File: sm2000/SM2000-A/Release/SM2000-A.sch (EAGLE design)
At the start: 455 parts, among them CN1 HDR100-3, CN2 ST-3509, CN3 HDR100-3, CN4 JS-MU3-002, CN5 DS-0518, CN6 ST-3509, CN7 ST-3509, J1 JMP-2PIN, J10 JMPR-2X2, J11 JMPR-2X2, J12 JMPR-2X2, J13 JMPR-2X2, J14 JMPR-2X2, J2 HDR100-7, J3 JMP-2PIN, J4 CONN-BOOM-XH-2A, J5 JMP-2PIN, J6 JMPR-2X2, J7 JMPR-2X2, J8 JMPR-2X2, J9 JMPR-2X2, P6 TPAD50, P7 TPAD50, P8 TPAD50, P9 TPAD50, Q1 MMBT3904, Q10 MMBT3904, Q11 BFR92, Q12 BFQ19, Q13 RD01MUS2, Q14 MMBT3904, Q15 MMBT3904, Q16 MMBT3904, Q17 MMBT3906, Q2 STR2P3LLH6, Q3 MMBT3904, Q4 STR2P3LLH6, Q5 MMBT3904, Q6 MMBT3904, Q7 MMBT3904, Q8 MMBT3904, Q9 MMBT3904, SW1 TS-02B, SW2 SW-LC2259, SW3 TS-026, SW4 TS-026, SW5 SW-LC2259EENP, U1 STM32F405VGT6, U10 LM386M-1, U11 ADE-1, U12 PGA-103+, U13 LMV341, U14 SI5351A, U15 SI570, U16 SA612A, U2 STMPS2141, U3 EMIF02-USB03F2, U4 DNL, U5 L78M09, U6 LD1117AS-33, U7 LMV341, U8 LD1117AS-33, U9 TPS54329E, X1 BU-SMA-H

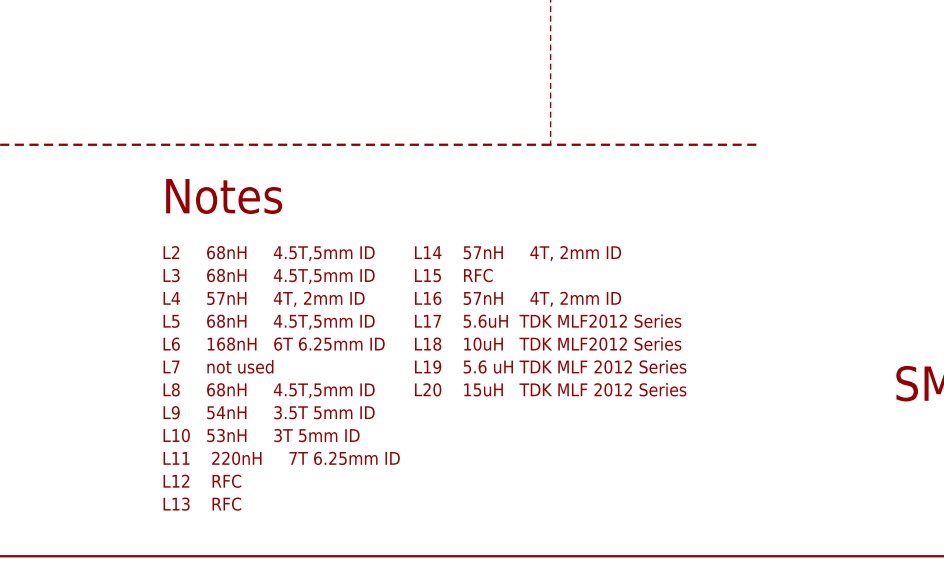
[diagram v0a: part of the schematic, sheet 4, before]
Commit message: SM2000-A Folders should now be current. RGB
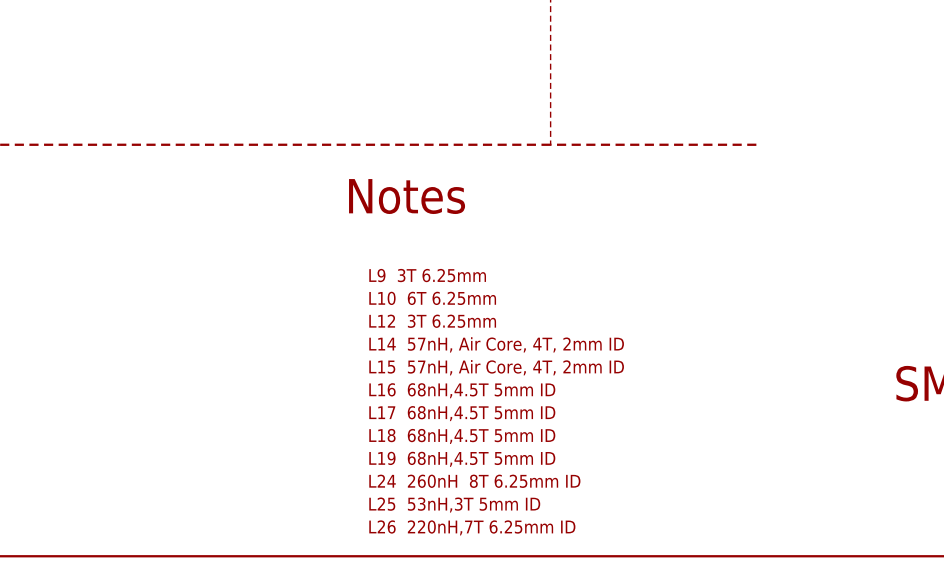
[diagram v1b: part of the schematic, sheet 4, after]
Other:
- note added: "L10 6T 6.25mm"
- note added: "L12 3T 6.25mm"
- note added: "L14 57nH, Air Core, 4T, 2mm ID"
- note added: "L15 57nH, Air Core, 4T, 2mm ID"
- note added: "L16 68nH,4.5T 5mm ID"
- note added: "L17 68nH,4.5T 5mm ID"
- note added: "L18 68nH,4.5T 5mm ID"
- note added: "L19 68nH,4.5T 5mm ID"
- note added: "L24 260nH 8T 6.25mm ID"
- note added: "L25 53nH,3T 5mm ID"
- note added: "L26 220nH,7T 6.25mm ID"
- note added: "L9 3T 6.25mm"
- note removed: "L10 53nH 3T 5mm ID"
- note removed: "L11 220nH 7T 6.25mm ID"
- note removed: "L12 RFC"
- note removed: "L13 RFC"
- note removed: "L14 57nH 4T, 2mm ID"
- note removed: "L15 RFC"
- note removed: "L16 57nH 4T, 2mm ID"
- note removed: "L17 5.6uH TDK MLF2012 Series"
- note removed: "L18 10uH TDK MLF2012 Series"
- note removed: "L19 5.6 uH TDK MLF 2012 Series"
- note removed: "L2 68nH 4.5T,5mm ID"
- note removed: "L20 15uH TDK MLF 2012 Series"
- note removed: "L3 68nH 4.5T,5mm ID"
- note removed: "L4 57nH 4T, 2mm ID"
- note removed: "L5 68nH 4.5T,5mm ID"
- note removed: "L6 168nH 6T 6.25mm ID"
- note removed: "L7 not used"
- note removed: "L8 68nH 4.5T,5mm ID"
- note removed: "L9 54nH 3.5T 5mm ID"
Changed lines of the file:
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@@
 <text x="345.44" y="17.272" size="3.81" layer="94" ratio="10">SM2000 - </text>
 <text x="422.148" y="6.35" size="3.81" layer="94" ratio="10">A</text>
+<text x="287.02" y="27.94" size="1.4224" layer="94">L10  6T 6.25mm</text>
+<text x="287.02" y="25.4" size="1.4224" layer="94">L12  3T 6.25mm</text>
+<text x="287.02" y="30.48" size="1.4224" layer="94">L9  3T 6.25mm</text>
+<text x="287.02" y="2.54" size="1.4224" layer="94" ratio="10">L26  220nH,7T 6.25mm ID</text>
+<text x="287.02" y="10.16" size="1.4224" layer="94" ratio="10">L19  68nH,4.5T 5mm ID</text>
+<text x="287.02" y="12.7" size="1.4224" layer="94" ratio="10">L18  68nH,4.5T 5mm ID</text>
+<text x="287.02" y="15.24" size="1.4224" layer="94" ratio="10">L17  68nH,4.5T 5mm ID</text>
+<text x="287.02" y="17.78" size="1.4224" layer="94" ratio="10">L16  68nH,4.5T 5mm ID</text>
+<text x="287.02" y="7.62" size="1.4224" layer="94" ratio="10">L24  260nH  8T 6.25mm ID</text>
+<text x="287.02" y="5.08" size="1.4224" layer="94" ratio="10">L25  53nH,3T 5mm ID</text>
+<text x="287.02" y="20.32" size="1.4224" layer="94" ratio="10">L15  57nH, Air Core, 4T, 2mm ID</text>
+<text x="287.02" y="22.86" size="1.4224" layer="94" ratio="10">L14  57nH, Air Core, 4T, 2mm ID</text>
 <text x="157.48" y="215.9" size="1.4224" layer="91">1.7V</text>
 <text x="147.32" y="215.9" size="1.4224" layer="91">1.4V</text>
@@
 <wire x1="307.34" y1="45.72" x2="187.96" y2="45.72" width="0.254" layer="94" style="longdash"/>
 <wire x1="187.96" y1="45.72" x2="147.32" y2="45.72" width="0.254" layer="94" style="longdash"/>
-<text x="264.16" y="38.1" size="3.81" layer="94" ratio="10">Notes</text>
+<text x="284.48" y="38.1" size="3.81" layer="94" ratio="10">Notes</text>
 <text x="259.08" y="104.14" size="1.4224" layer="94">To PA1 ADC uC</text>
 <text x="160.02" y="129.54" size="1.4224" layer="94">From 2nd Rx Mixer NE602</text>
@@
 <text x="53.34" y="160.02" size="3.81" layer="94" ratio="10">LOCAL OSCILLATOR</text>
 <wire x1="307.34" y1="175.26" x2="307.34" y2="45.72" width="0.1524" layer="94" style="longdash"/>
-<text x="264.16" y="33.02" size="1.4224" layer="94" ratio="10">L2     68nH     4.5T,5mm ID</text>
-<text x="264.16" y="30.48" size="1.4224" layer="94" ratio="10">L3     68nH     4.5T,5mm ID</text>
-<text x="264.16" y="25.4" size="1.4224" layer="94" ratio="10">L5     68nH     4.5T,5mm ID</text>
-<text x="264.16" y="17.78" size="1.4224" layer="94" ratio="10">L8     68nH     4.5T,5mm ID</text>
-<text x="264.16" y="27.94" size="1.4224" layer="94" ratio="10">L4     57nH     4T, 2mm ID</text>
-<text x="292.1" y="33.02" size="1.4224" layer="94" ratio="10">L14    57nH     4T, 2mm ID</text>
-<text x="292.1" y="27.94" size="1.4224" layer="94" ratio="10">L16    57nH     4T, 2mm ID</text>
-<text x="264.16" y="22.86" size="1.4224" layer="94" ratio="10">L6     168nH   6T 6.25mm ID</text>
-<text x="264.16" y="20.32" size="1.4224" layer="94" ratio="10">L7     not used</text>
-<text x="264.16" y="15.24" size="1.4224" layer="94" ratio="10">L9     54nH     3.5T 5mm ID</text>
-<text x="264.16" y="12.7" size="1.4224" layer="94" ratio="10">L10   53nH     3T 5mm ID</text>
-<text x="264.16" y="10.16" size="1.4224" layer="94" ratio="10">L11    220nH     7T 6.25mm ID</text>
-<text x="264.16" y="7.62" size="1.4224" layer="94" ratio="10">L12    RFC</text>
-<text x="264.16" y="5.08" size="1.4224" layer="94" ratio="10">L13    RFC</text>
-<text x="292.1" y="30.48" size="1.4224" layer="94" ratio="10">L15    RFC</text>
-<text x="292.1" y="25.4" size="1.4224" layer="94" ratio="10">L17    5.6uH  TDK MLF2012 Series</text>
-<text x="292.1" y="22.86" size="1.4224" layer="94" ratio="10">L18    10uH   TDK MLF2012 Series</text>
-<text x="292.1" y="20.32" size="1.4224" layer="94" ratio="10">L19    5.6 uH TDK MLF 2012 Series</text>
-<text x="292.1" y="17.78" size="1.4224" layer="94" ratio="10">L20    15uH   TDK MLF 2012 Series</text>
 </plain>
 <instances>
